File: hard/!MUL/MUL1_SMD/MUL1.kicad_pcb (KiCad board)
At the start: 2 copper layers, 83.8 x 36.2 mm, 13 parts, among them J1 Conn_01x08_Male, J2 Conn_01x09_Male, J3 Conn_01x08_Male, J4 Conn_01x01_Male, J5 Conn_01x02_Male, J6 Conn_01x01_Male, U1 74LS08, U2 74LS283, U3 74LS08, U4 74LS283

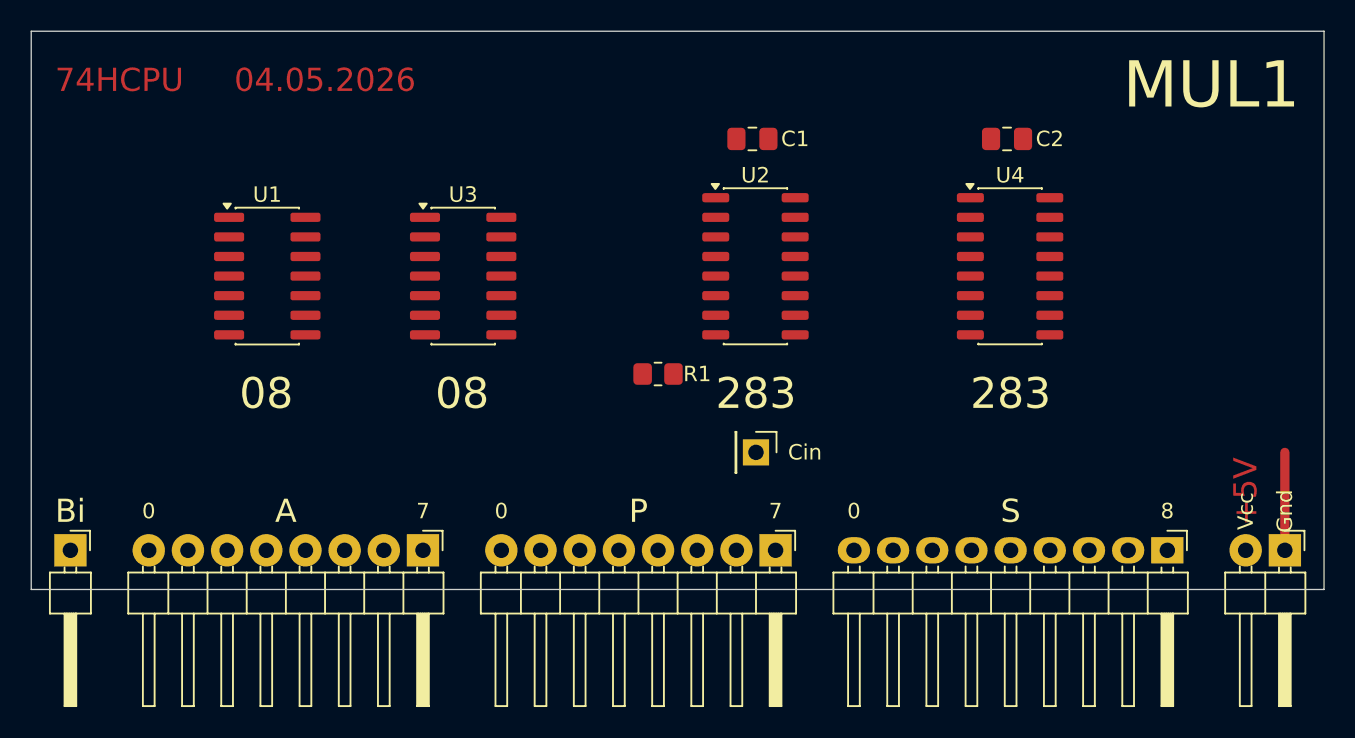
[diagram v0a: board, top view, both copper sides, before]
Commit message: 2 DIP and 2 SO!
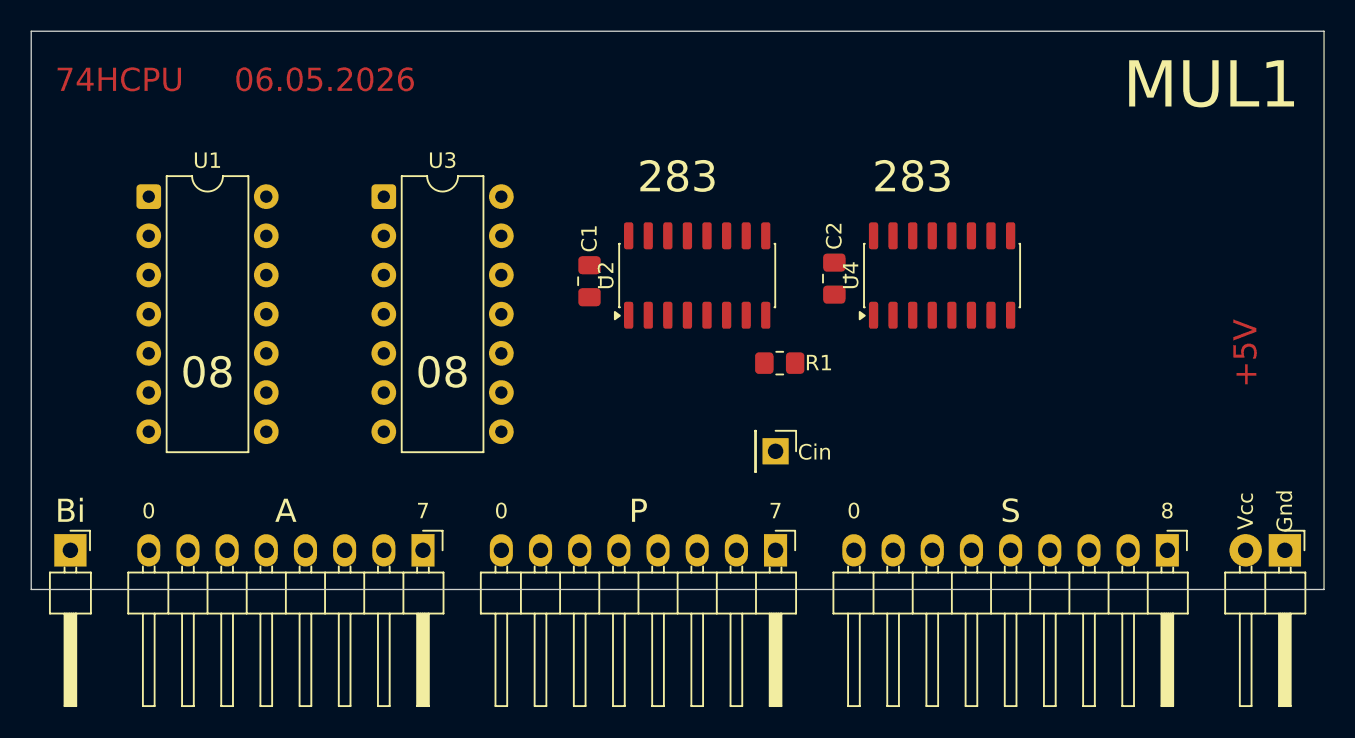
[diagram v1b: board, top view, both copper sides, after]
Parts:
- U1, U3: footprint Package_SO:SO-14_3.9x8.65mm_P1.27mm -> Package_DIP:DIP-14_W7.62mm
- moved C2 14.4 mm to (80.0, 43.4), turned to -90 degrees
- moved C1 14.0 mm to (64.1, 43.6), turned to -90 degrees
- moved U1 9.25 mm to (35.6, 38.1)
- moved R1 7.92 mm to (76.5, 48.9)
- moved U3 7.28 mm to (50.8, 38.1)
- moved U4 4.45 mm to (87.0, 43.2), turned to 90 degrees
- moved U2 3.82 mm to (71.1, 43.2), turned to 90 degrees
- moved J6 1.27 mm to (76.2, 54.6)
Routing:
- net GND: track 6.35 -> 0.00 mm
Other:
- board text added: "06.05.2026"
- board text removed: "04.05.2026"
